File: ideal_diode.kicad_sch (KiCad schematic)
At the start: 5 parts, among them Q3 BSC059N04LS6, U14 LM74700

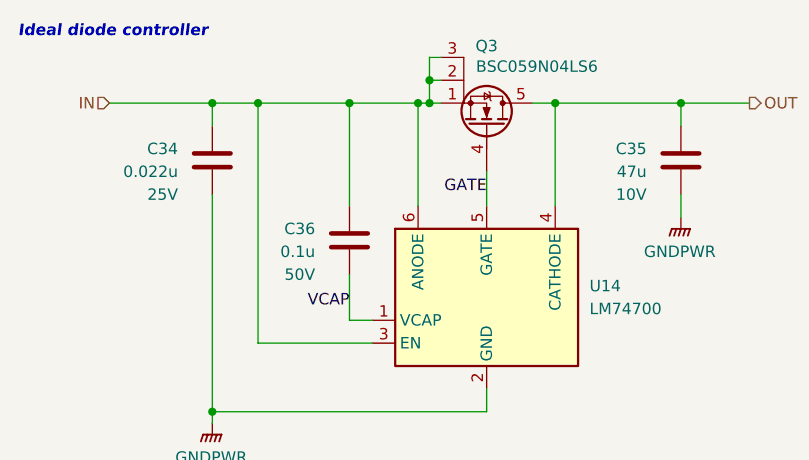
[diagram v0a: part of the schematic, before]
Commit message: Begin layout
Completed ideal diode layout
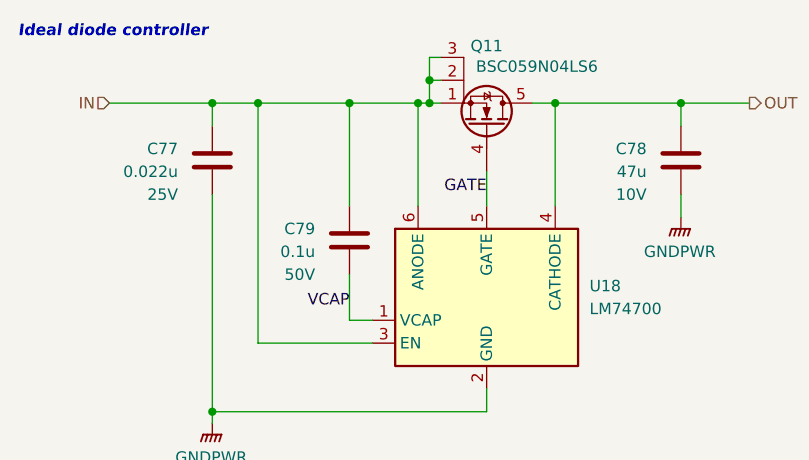
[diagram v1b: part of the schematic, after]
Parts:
- renumbered C34 to C77, C35 to C78, C36 to C79, Q3 to Q11, U14 to U18
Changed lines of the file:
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@@
 		(on_board yes)
 		(dnp no)
-		(property "Reference" "C35"
+		(property "Reference" "C78"
 			(at 121.92 36.8299 0)
 			(effects
@@
 		(on_board yes)
 		(dnp no)
-		(property "Reference" "C34"
+		(property "Reference" "C77"
 			(at 69.85 36.8299 0)
 			(effects
@@
 		(dnp no)
 		(fields_autoplaced yes)
-		(property "Reference" "#PWR095"
+		(property "Reference" "#PWR0104"
 			(at 73.66 72.39 0)
 			(effects
@@
 		(on_board yes)
 		(dnp no)
-		(property "Reference" "C36"
+		(property "Reference" "C79"
 			(at 85.09 45.7199 0)
 			(effects
@@
 		(on_board yes)
 		(dnp no)
-		(property "Reference" "Q3"
+		(property "Reference" "Q11"
 			(at 104.14 25.4 90)
 			(effects
@@
 		(dnp no)
 		(fields_autoplaced yes)
-		(property "Reference" "U14"
+		(property "Reference" "U18"
 			(at 115.57 52.0699 0)
 			(effects
@@
 		(dnp no)
 		(fields_autoplaced yes)
-		(property "Reference" "#PWR094"
+		(property "Reference" "#PWR0103"
 			(at 125.73 49.53 0)
 			(effects

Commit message: Unsure of changes
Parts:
- renumbered C77 to C34, C78 to C35, C79 to C36, Q11 to Q3, U18 to U14
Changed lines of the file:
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@@
 		(on_board yes)
 		(dnp no)
-		(property "Reference" "C78"
+		(property "Reference" "C35"
 			(at 121.92 36.8299 0)
 			(effects
@@
 		(on_board yes)
 		(dnp no)
-		(property "Reference" "C77"
+		(property "Reference" "C34"
 			(at 69.85 36.8299 0)
 			(effects
@@
 		(dnp no)
 		(fields_autoplaced yes)
-		(property "Reference" "#PWR0104"
+		(property "Reference" "#PWR095"
 			(at 73.66 72.39 0)
 			(effects
@@
 		(on_board yes)
 		(dnp no)
-		(property "Reference" "C79"
+		(property "Reference" "C36"
 			(at 85.09 45.7199 0)
 			(effects
@@
 		(on_board yes)
 		(dnp no)
-		(property "Reference" "Q11"
+		(property "Reference" "Q3"
 			(at 104.14 25.4 90)
 			(effects
@@
 		(dnp no)
 		(fields_autoplaced yes)
-		(property "Reference" "U18"
+		(property "Reference" "U14"
 			(at 115.57 52.0699 0)
 			(effects
@@
 		(dnp no)
 		(fields_autoplaced yes)
-		(property "Reference" "#PWR0103"
+		(property "Reference" "#PWR094"
 			(at 125.73 49.53 0)
 			(effects
